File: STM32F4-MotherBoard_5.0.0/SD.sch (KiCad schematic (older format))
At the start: 4 parts

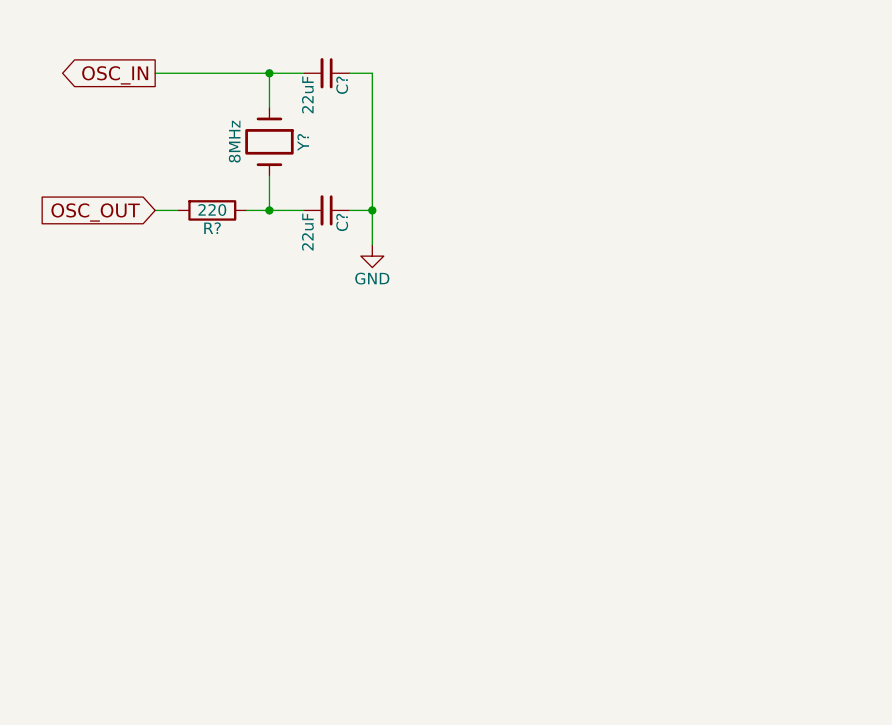
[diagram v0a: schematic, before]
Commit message: SDとCANの追加とラベルミス修正
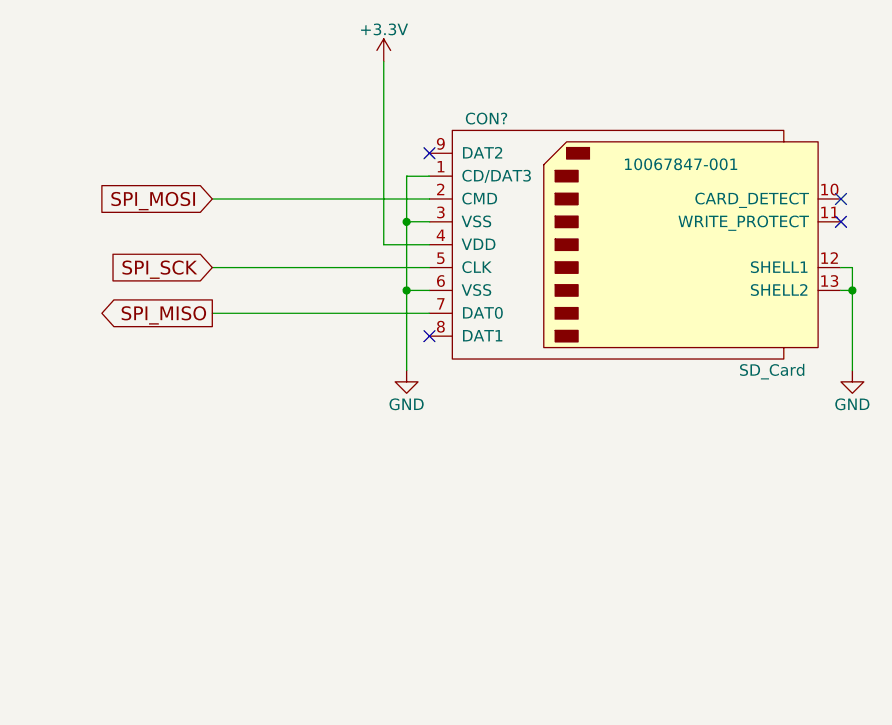
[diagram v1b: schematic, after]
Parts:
- removed C? (x2): 22uF, symbol C_Small
- removed R?: 220, symbol R
- removed Y?: 8MHz, symbol Crystal
- added CON?: SD_Card, 10067847-001, symbol SD_Card
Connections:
- net GND: now also CON?.1 (CD/DAT3), CON?.12 (SHELL1), CON?.13 (SHELL2), CON?.3 (VSS), CON?.6 (VSS)
- new net +3V3: CON?.4 (VDD)
- new net SPI_MISO: CON?.7 (DAT0)
- new net SPI_MOSI: CON?.2 (CMD)
- new net SPI_SCK: CON?.5 (CLK)
- no-connect marks 0 -> 4
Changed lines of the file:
@@
 $Descr A4 11693 8268
 encoding utf-8
-Sheet 9 11
+Sheet 11 11
 Title ""
 Date ""
@@
 Comment4 ""
 $EndDescr
-Text GLabel 4100 2500 0    60   Output ~ 0
-OSC_IN
-Text GLabel 4100 3100 0    60   Input ~ 0
-OSC_OUT
+Text GLabel 4350 3350 0    60   Input ~ 0
+SPI_SCK
+Text GLabel 4350 3050 0    60   Input ~ 0
+SPI_MOSI
+Text GLabel 4350 3550 0    60   Output ~ 0
+SPI_MISO
 $Comp
-L Crystal Y?
-U 1 1 589F7562
-P 4600 2800
-F 0 "Y?" H 4600 2950 50  0000 C CNN
-F 1 "8MHz" H 4600 2650 50  0000 C CNN
-F 2 "" H 4600 2800 50  0000 C CNN
-F 3 "" H 4600 2800 50  0000 C CNN
-	1    4600 2800
-	0    1    1    0
+L SD_Card CON?
+U 1 1 58A2FDC9
+P 6200 3250
+F 0 "CON?" H 5550 3800 50  0000 C CNN
+F 1 "SD_Card" H 6800 2700 50  0000 C CNN
+F 2 "10067847-001" H 6400 3600 50  0000 C CNN
+F 3 "" H 6200 3250 50  0000 C CNN
+	1    6200 3250
+	1    0    0    -1
 $EndComp
 Wire Wire Line
-	4100 2500 4750 2500
+	5300 3550 4350 3550
 Wire Wire Line
-	4600 2500 4600 2650
+	4350 3050 5300 3050
 Wire Wire Line
-	4600 2950 4600 3100
+	4350 3350 5300 3350
+Wire Wire Line
+	5300 2950 5200 2950
+Wire Wire Line
+	5200 2950 5200 3800
 $Comp
-L R R?
-U 1 1 589F75A6
-P 4350 3100
-F 0 "R?" V 4430 3100 50  0000 C CNN
-F 1 "220" V 4350 3100 50  0000 C CNN
-F 2 "" V 4280 3100 50  0000 C CNN
-F 3 "" H 4350 3100 50  0000 C CNN
-	1    4350 3100
-	0    1    1    0
+L GND #PWR?
+U 1 1 58A2FE1C
+P 5200 3800
+F 0 "#PWR?" H 5200 3550 50  0001 C CNN
+F 1 "GND" H 5200 3650 50  0000 C CNN
+F 2 "" H 5200 3800 50  0000 C CNN
+F 3 "" H 5200 3800 50  0000 C CNN
+	1    5200 3800
+	1    0    0    -1
 $EndComp
 Wire Wire Line
-	4200 3100 4100 3100
+	5300 3150 5200 3150
+Connection ~ 5200 3150
+$Comp
+L +3.3V #PWR?
+U 1 1 58A2FE3B
+P 5100 2450
+F 0 "#PWR?" H 5100 2300 50  0001 C CNN
+F 1 "+3.3V" H 5100 2590 50  0000 C CNN
+F 2 "" H 5100 2450 50  0000 C CNN
+F 3 "" H 5100 2450 50  0000 C CNN
+	1    5100 2450
+	1    0    0    -1
+$EndComp
 Wire Wire Line
-	4500 3100 4750 3100
-$Comp
-L C_Small C?
-U 1 1 589F75D2
-P 4850 3100
-F 0 "C?" H 4860 3170 50  0000 L CNN
-F 1 "22uF" H 4860 3020 50  0000 L CNN
-F 2 "" H 4850 3100 50  0000 C CNN
-F 3 "" H 4850 3100 50  0000 C CNN
-	1    4850 3100
-	0    1    1    0
-$EndComp
-$Comp
-L C_Small C?
-U 1 1 589F75F6
-P 4850 2500
-F 0 "C?" H 4860 2570 50  0000 L CNN
-F 1 "22uF" H 4860 2420 50  0000 L CNN
-F 2 "" H 4850 2500 50  0000 C CNN
-F 3 "" H 4850 2500 50  0000 C CNN
-	1    4850 2500
-	0    1    1    0
-$EndComp
-Connection ~ 4600 2500
-Connection ~ 4600 3100
+	5100 2450 5100 3250
 Wire Wire Line
-	4950 3100 5050 3100
+	5100 3250 5300 3250
 Wire Wire Line
-	5050 2500 5050 3250
+	5300 3450 5200 3450
+Connection ~ 5200 3450
+NoConn ~ 5300 2850
+NoConn ~ 5300 3650
+NoConn ~ 7100 3050
+NoConn ~ 7100 3150
 Wire Wire Line
-	5050 2500 4950 2500
-Connection ~ 5050 3100
+	7100 3350 7150 3350
+Wire Wire Line
+	7150 3350 7150 3800
+Wire Wire Line
+	7150 3450 7100 3450
+Connection ~ 7150 3450
 $Comp
 L GND #PWR?
-U 1 1 589F765B
-P 5050 3250
-F 0 "#PWR?" H 5050 3000 50  0001 C CNN
-F 1 "GND" H 5050 3100 50  0000 C CNN
-F 2 "" H 5050 3250 50  0000 C CNN
-F 3 "" H 5050 3250 50  0000 C CNN
-	1    5050 3250
+U 1 1 58A2FEA7
+P 7150 3800
+F 0 "#PWR?" H 7150 3550 50  0001 C CNN
+F 1 "GND" H 7150 3650 50  0000 C CNN
+F 2 "" H 7150 3800 50  0000 C CNN
+F 3 "" H 7150 3800 50  0000 C CNN
+	1    7150 3800
 	1    0    0    -1
 $EndComp

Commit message: 回路図終わり
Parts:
- gave numbers to parts that had none: 1
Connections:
- net GND: no longer CON1.1 (CD/DAT3)
- new net SPI_CS: CON1.1 (CD/DAT3)
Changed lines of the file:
@@
 $Descr A4 11693 8268
 encoding utf-8
-Sheet 11 11
+Sheet 11 12
 Title ""
 Date ""
@@
 SPI_MISO
 $Comp
-L SD_Card CON?
+L SD_Card CON1
 U 1 1 58A2FDC9
 P 6200 3250
-F 0 "CON?" H 5550 3800 50  0000 C CNN
+F 0 "CON1" H 5550 3800 50  0000 C CNN
 F 1 "SD_Card" H 6800 2700 50  0000 C CNN
 F 2 "10067847-001" H 6400 3600 50  0000 C CNN
@@
 	4350 3350 5300 3350
 Wire Wire Line
-	5300 2950 5200 2950
-Wire Wire Line
-	5200 2950 5200 3800
+	4650 2950 5300 2950
 $Comp
-L GND #PWR?
+L GND #PWR066
 U 1 1 58A2FE1C
 P 5200 3800
-F 0 "#PWR?" H 5200 3550 50  0001 C CNN
+F 0 "#PWR066" H 5200 3550 50  0001 C CNN
 F 1 "GND" H 5200 3650 50  0000 C CNN
 F 2 "" H 5200 3800 50  0000 C CNN
@@
 Wire Wire Line
 	5300 3150 5200 3150
-Connection ~ 5200 3150
 $Comp
-L +3.3V #PWR?
+L +3.3V #PWR067
 U 1 1 58A2FE3B
 P 5100 2450
-F 0 "#PWR?" H 5100 2300 50  0001 C CNN
+F 0 "#PWR067" H 5100 2300 50  0001 C CNN
 F 1 "+3.3V" H 5100 2590 50  0000 C CNN
 F 2 "" H 5100 2450 50  0000 C CNN
@@
 Connection ~ 7150 3450
 $Comp
-L GND #PWR?
+L GND #PWR068
 U 1 1 58A2FEA7
 P 7150 3800
-F 0 "#PWR?" H 7150 3550 50  0001 C CNN
+F 0 "#PWR068" H 7150 3550 50  0001 C CNN
 F 1 "GND" H 7150 3650 50  0000 C CNN
 F 2 "" H 7150 3800 50  0000 C CNN
@@
 	1    0    0    -1
 $EndComp
+Wire Wire Line
+	5200 3150 5200 3800
+Wire Wire Line
+	4650 2950 4650 2850
+Wire Wire Line
+	4650 2850 4350 2850
+Text GLabel 4350 2850 0    60   Input ~ 0
+SPI_CS
 $EndSCHEMATC

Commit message: replace project
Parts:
- removed CON1: SD_Card, 10067847-001, symbol SD_Card
- added J5: DM3AT-SF-PEJM5, DM3AT-SF-PEJM5:HRS_DM3AT-SF-PEJM5, symbol DM3AT-SF-PEJM5
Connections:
- net +3V3: now also J5.4 (VCC)
- net GND: now also J5.6 (GND)
- net SPI_CS: now also J5.2 (DATA3-CD/CS)
- net SPI_MISO: now also J5.7 (DATA0/DO)
- net SPI_MOSI: now also J5.3 (CMD/DI)
- net SPI_SCK: now also J5.5 (CLK)
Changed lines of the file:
@@
 LIBS:STM32F4-MotherBoard_3.0.0-cache
 LIBS:STM32F4-MotherBoard_5.0.0-cache
+LIBS:DM3AT-SF-PEJM5
 EELAYER 25 0
 EELAYER END
@@
 Comment4 ""
 $EndDescr
-Text GLabel 4350 3350 0    60   Input ~ 0
+Text GLabel 4350 4600 0    60   Input ~ 0
 SPI_SCK
-Text GLabel 4350 3050 0    60   Input ~ 0
+Text GLabel 4350 4500 0    60   Input ~ 0
 SPI_MOSI
-Text GLabel 4350 3550 0    60   Output ~ 0
+Text GLabel 4350 4100 0    60   Output ~ 0
 SPI_MISO
+Wire Wire Line
+	5300 4100 4350 4100
+Wire Wire Line
+	4350 4500 5300 4500
+Wire Wire Line
+	4350 4600 5300 4600
+Wire Wire Line
+	4350 4400 5300 4400
 $Comp
-L SD_Card CON1
-U 1 1 58A2FDC9
-P 6200 3250
-F 0 "CON1" H 5550 3800 50  0000 C CNN
-F 1 "SD_Card" H 6800 2700 50  0000 C CNN
-F 2 "10067847-001" H 6400 3600 50  0000 C CNN
-F 3 "" H 6200 3250 50  0000 C CNN
-	1    6200 3250
+L GND #PWR072
+U 1 1 58A2FE1C
+P 5200 5050
+F 0 "#PWR072" H 5200 4800 50  0001 C CNN
+F 1 "GND" H 5200 4900 50  0000 C CNN
+F 2 "" H 5200 5050 50  0000 C CNN
+F 3 "" H 5200 5050 50  0000 C CNN
+	1    5200 5050
+	1    0    0    -1
+$EndComp
+$Comp
+L +3.3V #PWR073
+U 1 1 58A2FE3B
+P 5100 3950
+F 0 "#PWR073" H 5100 3800 50  0001 C CNN
+F 1 "+3.3V" H 5100 4090 50  0000 C CNN
+F 2 "" H 5100 3950 50  0000 C CNN
+F 3 "" H 5100 3950 50  0000 C CNN
+	1    5100 3950
 	1    0    0    -1
 $EndComp
 Wire Wire Line
-	5300 3550 4350 3550
+	5100 4000 5300 4000
 Wire Wire Line
-	4350 3050 5300 3050
-Wire Wire Line
-	4350 3350 5300 3350
-Wire Wire Line
-	4650 2950 5300 2950
+	5300 4700 5200 4700
+NoConn ~ 5300 4200
+Text GLabel 4350 4400 0    60   Input ~ 0
+SPI_CS
+NoConn ~ 5300 4300
 $Comp
-L GND #PWR072
-U 1 1 58A2FE1C
-P 5200 3800
-F 0 "#PWR072" H 5200 3550 50  0001 C CNN
-F 1 "GND" H 5200 3650 50  0000 C CNN
-F 2 "" H 5200 3800 50  0000 C CNN
-F 3 "" H 5200 3800 50  0000 C CNN
-	1    5200 3800
+L DM3AT-SF-PEJM5 J5
+U 1 1 58DE04A7
+P 5500 4500
+F 0 "J5" H 5500 5120 50  0000 L CNN
+F 1 "DM3AT-SF-PEJM5" H 5500 3780 50  0000 L CNN
+F 2 "DM3AT-SF-PEJM5:HRS_DM3AT-SF-PEJM5" H 5500 4500 50  0001 L CNN
+F 3 "DM3AT-SF-PEJM5" H 5500 4500 50  0001 L CNN
+F 4 "Good" H 5500 4500 50  0001 L CNN "Availability"
+F 5 "DM3 Series 8 Position Right Angle SMT Push Push Ejection MicroSD Card Connector" H 5500 4500 50  0001 L CNN "Description"
+F 6 "None" H 5500 4500 50  0001 L CNN "Package"
+F 7 "Hirose" H 5500 4500 50  0001 L CNN "MF"
+F 8 "1.96 USD" H 5500 4500 50  0001 L CNN "Price"
+	1    5500 4500
 	1    0    0    -1
 $EndComp
 Wire Wire Line
-	5300 3150 5200 3150
-$Comp
-L +3.3V #PWR073
-U 1 1 58A2FE3B
-P 5100 2450
-F 0 "#PWR073" H 5100 2300 50  0001 C CNN
-F 1 "+3.3V" H 5100 2590 50  0000 C CNN
-F 2 "" H 5100 2450 50  0000 C CNN
-F 3 "" H 5100 2450 50  0000 C CNN
-	1    5100 2450
-	1    0    0    -1
-$EndComp
+	5200 4700 5200 5050
 Wire Wire Line
-	5100 2450 5100 3250
-Wire Wire Line
-	5100 3250 5300 3250
-Wire Wire Line
-	5300 3450 5200 3450
-Connection ~ 5200 3450
-NoConn ~ 5300 2850
-NoConn ~ 5300 3650
-NoConn ~ 7100 3050
-NoConn ~ 7100 3150
-Wire Wire Line
-	7100 3350 7150 3350
-Wire Wire Line
-	7150 3350 7150 3800
-Wire Wire Line
-	7150 3450 7100 3450
-Connection ~ 7150 3450
-$Comp
-L GND #PWR074
-U 1 1 58A2FEA7
-P 7150 3800
-F 0 "#PWR074" H 7150 3550 50  0001 C CNN
-F 1 "GND" H 7150 3650 50  0000 C CNN
-F 2 "" H 7150 3800 50  0000 C CNN
-F 3 "" H 7150 3800 50  0000 C CNN
-	1    7150 3800
-	1    0    0    -1
-$EndComp
-Wire Wire Line
-	5200 3150 5200 3800
-Wire Wire Line
-	4650 2950 4650 2850
-Wire Wire Line
-	4650 2850 4350 2850
-Text GLabel 4350 2850 0    60   Input ~ 0
-SPI_CS
+	5100 4000 5100 3950
+NoConn ~ 5300 4900
+NoConn ~ 5300 5000
 $EndSCHEMATC
